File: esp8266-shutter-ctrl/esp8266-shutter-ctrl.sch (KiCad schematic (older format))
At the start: 6 parts

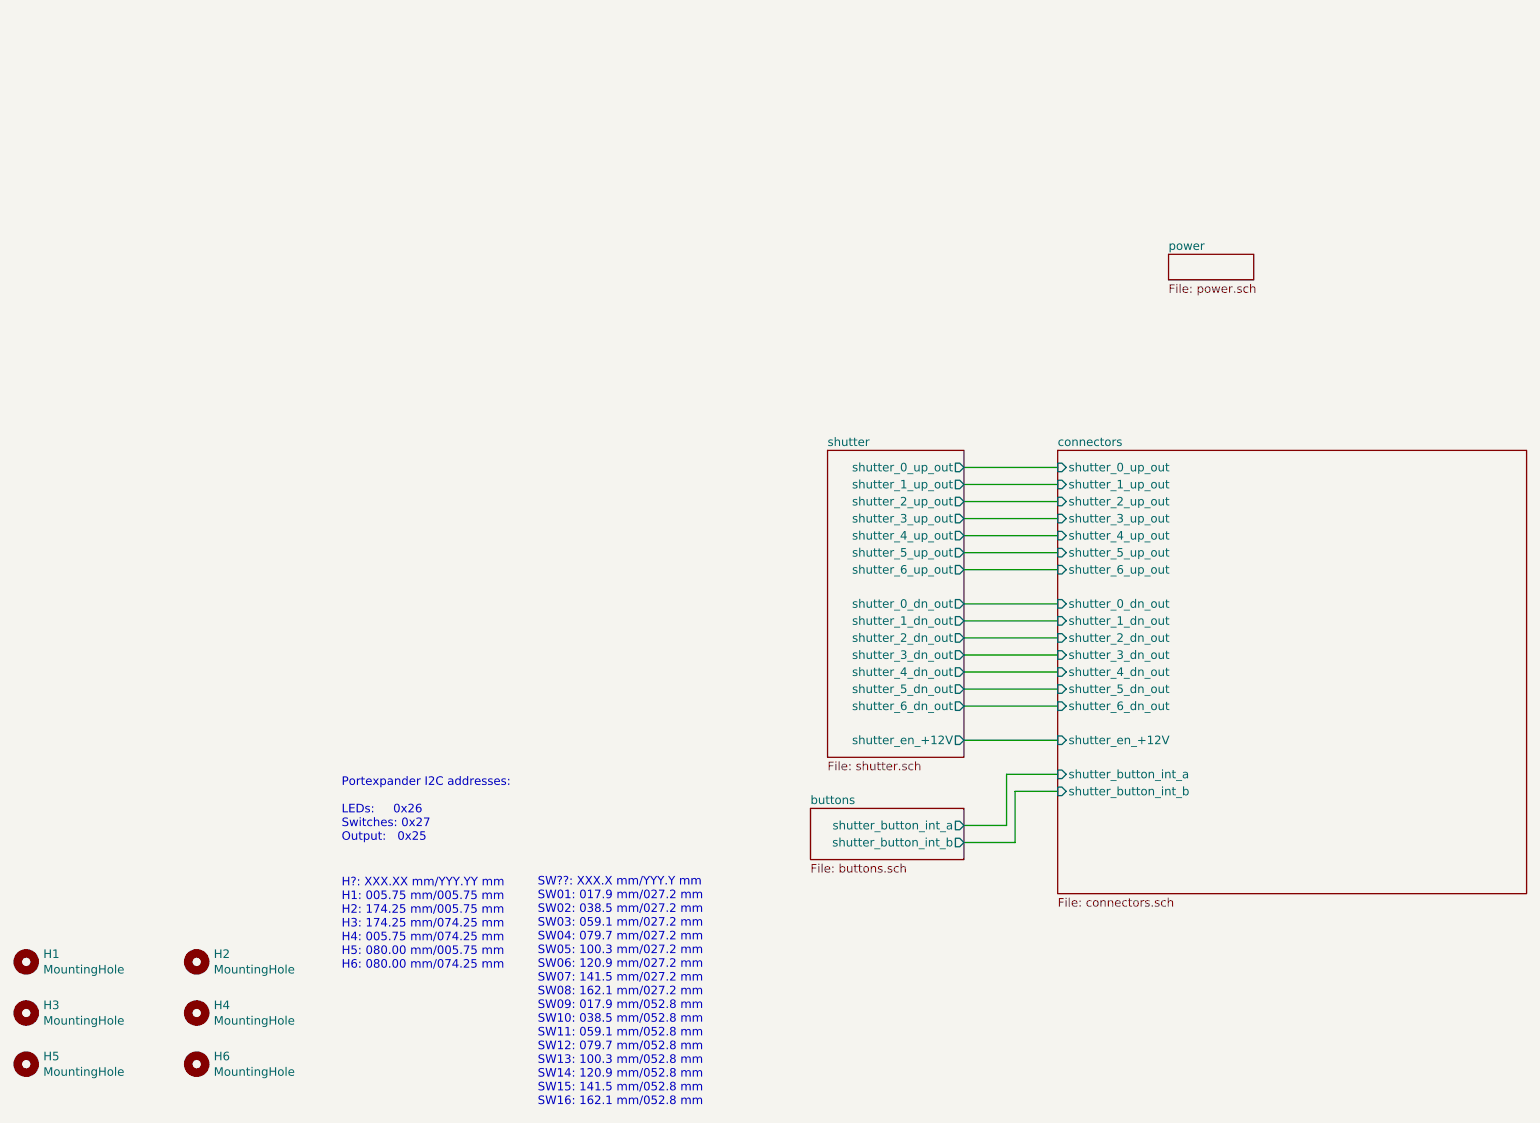
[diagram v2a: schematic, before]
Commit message: shutter-ctrl: sch: updated comments and titles
Signed-off-by: Dominik Laton <dominik.laton@web.de>
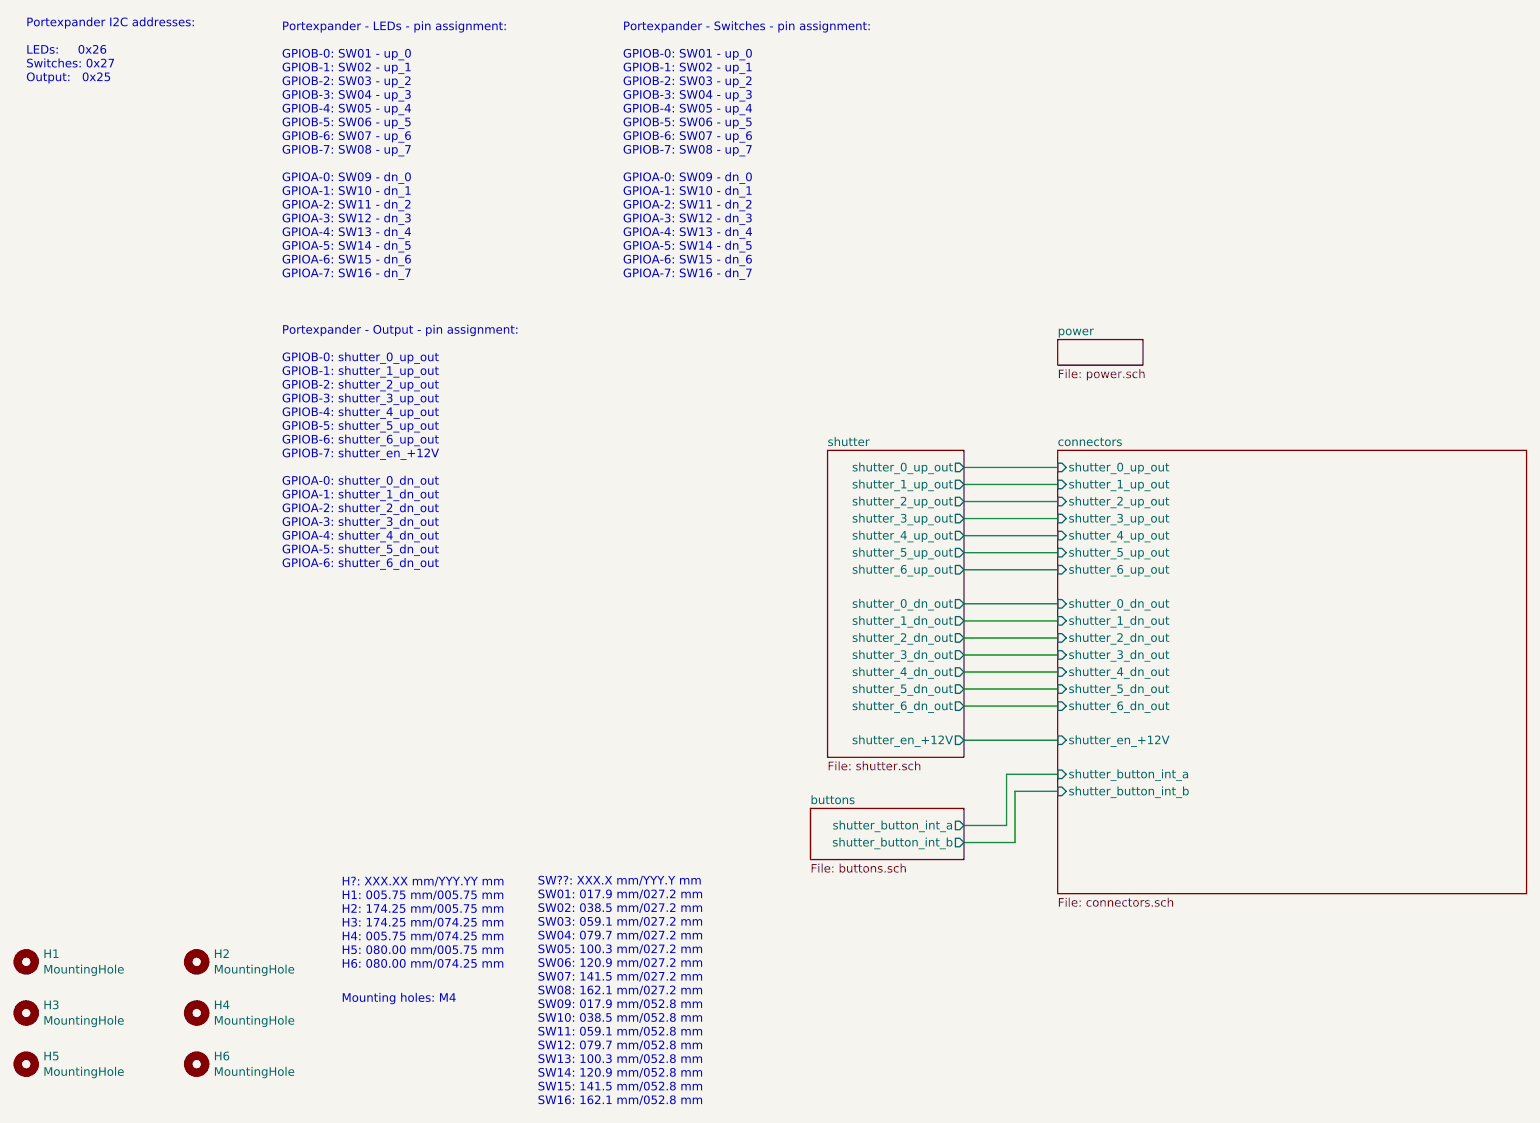
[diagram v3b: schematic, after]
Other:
- note added: "Mounting holes: M4"
- note added: "Portexpander - LEDs - pin assignment:\n\nGPIOB-0: SW01 - up_0\nGPIOB-1: SW02 - up_1\nGPIOB-2: SW03 - up_2\nGPIOB-3: SW04 - up_3\nGPIOB-4: SW05 - up_4\nGPIOB-5: SW06 - up_5\nGPIOB-6: SW07 - up_6\nGPIOB-7: SW08 - up_7\n\nGPIOA-0: SW09 - dn_0\nGPIOA-1: SW10 - dn_1\nGPIOA-2: SW11 - dn_2\nGPIOA-3: SW12 - dn_3\nGPIOA-4: SW13 - dn_4\nGPIOA-5: SW14 - dn_5\nGPIOA-6: SW15 - dn_6\nGPIOA-7: SW16 - dn_7"
- note added: "Portexpander - Output - pin assignment:\n\nGPIOB-0: shutter_0_up_out\nGPIOB-1: shutter_1_up_out\nGPIOB-2: shutter_2_up_out\nGPIOB-3: shutter_3_up_out\nGPIOB-4: shutter_4_up_out\nGPIOB-5: shutter_5_up_out\nGPIOB-6: shutter_6_up_out\nGPIOB-7: shutter_en_+12V\n\nGPIOA-0: shutter_0_dn_out\nGPIOA-1: shutter_1_dn_out\nGPIOA-2: shutter_2_dn_out\nGPIOA-3: shutter_3_dn_out\nGPIOA-4: shutter_4_dn_out\nGPIO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"
- note added: "Portexpander - Switches - pin assignment:\n\nGPIOB-0: SW01 - up_0\nGPIOB-1: SW02 - up_1\nGPIOB-2: SW03 - up_2\nGPIOB-3: SW04 - up_3\nGPIOB-4: SW05 - up_4\nGPIOB-5: SW06 - up_5\nGPIOB-6: SW07 - up_6\nGPIOB-7: SW08 - up_7\n\nGPIOA-0: SW09 - dn_0\nGPIOA-1: SW10 - dn_1\nGPIOA-2: SW11 - dn_2\nGPIOA-3: SW12 - dn_3\nGPIOA-4: SW13 - dn_4\nGPIOA-5: SW14 - dn_5\nGPIOA-6: SW15 - dn_6\nGPIOA-7: SW16 - dn_7"
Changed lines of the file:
@@
 $EndSheet
 $Sheet
-S 7700 2350 500  150
+S 7050 2850 500  150
 U 5FCBAC22
 F0 "power" 50
@@
 Text Notes 2850 6550 0    50   ~ 0
 H?: XXX.XX mm/YYY.YY mm\nH1: 005.75 mm/005.75 mm\nH2: 174.25 mm/005.75 mm\nH3: 174.25 mm/074.25 mm\nH4: 005.75 mm/074.25 mm\nH5: 080.00 mm/005.75 mm\nH6: 080.00 mm/074.25 mm
-Text Notes 2850 5800 0    50   ~ 0
+Text Notes 1000 1350 0    50   ~ 0
 Portexpander I2C addresses:\n\nLEDs:     0x26\nSwitches: 0x27\nOutput:   0x25
 Text Notes 4000 7350 0    50   ~ 0
 SW??: XXX.X mm/YYY.Y mm\nSW01: 017.9 mm/027.2 mm\nSW02: 038.5 mm/027.2 mm\nSW03: 059.1 mm/027.2 mm\nSW04: 079.7 mm/027.2 mm\nSW05: 100.3 mm/027.2 mm\nSW06: 120.9 mm/027.2 mm\nSW07: 141.5 mm/027.2 mm\nSW08: 162.1 mm/027.2 mm\nSW09: 017.9 mm/052.8 mm\nSW10: 038.5 mm/052.8 mm\nSW11: 059.1 mm/052.8 mm\nSW12: 079.7 mm/052.8 mm\nSW13: 100.3 mm/052.8 mm\nSW14: 120.9 mm/052.8 mm\nSW15: 141.5 mm/052.8 mm\nSW16: 162.1 mm/052.8 mm
+Text Notes 2850 6750 0    50   ~ 0
+Mounting holes: M4
+Text Notes 2500 4200 0    50   ~ 0
+Portexpander - Output - pin assignment:\n\nGPIOB-0: shutter_0_up_out\nGPIOB-1: shutter_1_up_out\nGPIOB-2: shutter_2_up_out\nGPIOB-3: shutter_3_up_out\nGPIOB-4: shutter_4_up_out\nGPIOB-5: shutter_5_up_out\nGPIOB-6: shutter_6_up_out\nGPIOB-7: shutter_en_+12V\n\nGPIOA-0: shutter_0_dn_out\nGPIOA-1: shutter_1_dn_out\nGPIOA-2: shutter_2_dn_out\nGPIOA-3: shutter_3_dn_out\nGPIOA-4: shutter_4_dn_out\nGPIOA-5: shutter_5_dn_out\nGPIOA-6: shutter_6_dn_out
+Text Notes 4500 2500 0    50   ~ 0
+Portexpander - Switches - pin assignment:\n\nGPIOB-0: SW01 - up_0\nGPIOB-1: SW02 - up_1\nGPIOB-2: SW03 - up_2\nGPIOB-3: SW04 - up_3\nGPIOB-4: SW05 - up_4\nGPIOB-5: SW06 - up_5\nGPIOB-6: SW07 - up_6\nGPIOB-7: SW08 - up_7\n\nGPIOA-0: SW09 - dn_0\nGPIOA-1: SW10 - dn_1\nGPIOA-2: SW11 - dn_2\nGPIOA-3: SW12 - dn_3\nGPIOA-4: SW13 - dn_4\nGPIOA-5: SW14 - dn_5\nGPIOA-6: SW15 - dn_6\nGPIOA-7: SW16 - dn_7
+Text Notes 2500 2500 0    50   ~ 0
+Portexpander - LEDs - pin assignment:\n\nGPIOB-0: SW01 - up_0\nGPIOB-1: SW02 - up_1\nGPIOB-2: SW03 - up_2\nGPIOB-3: SW04 - up_3\nGPIOB-4: SW05 - up_4\nGPIOB-5: SW06 - up_5\nGPIOB-6: SW07 - up_6\nGPIOB-7: SW08 - up_7\n\nGPIOA-0: SW09 - dn_0\nGPIOA-1: SW10 - dn_1\nGPIOA-2: SW11 - dn_2\nGPIOA-3: SW12 - dn_3\nGPIOA-4: SW13 - dn_4\nGPIOA-5: SW14 - dn_5\nGPIOA-6: SW15 - dn_6\nGPIOA-7: SW16 - dn_7
 $EndSCHEMATC
